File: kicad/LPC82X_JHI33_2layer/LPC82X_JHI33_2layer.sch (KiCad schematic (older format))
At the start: 24 parts, among them J1 Conn_02x09_Odd_Even, J2 Conn_02x09_Odd_Even, J3 JTAG_2X05, U1 LPC824M201JHI33, Y1 12MHz

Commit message: updated version number
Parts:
- N2: value 20181122 -> 20181123
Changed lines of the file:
@@
 P 4000 1650
 F 0 "N2" H 4000 1750 60  0000 C CNN
-F 1 "20181122" H 4000 1650 60  0000 C CNN
+F 1 "20181123" H 4000 1650 60  0000 C CNN
 F 2 "SquantorLabels:Label_version" H 4000 1650 60  0001 C CNN
 F 3 "" H 4000 1650 60  0001 C CNN

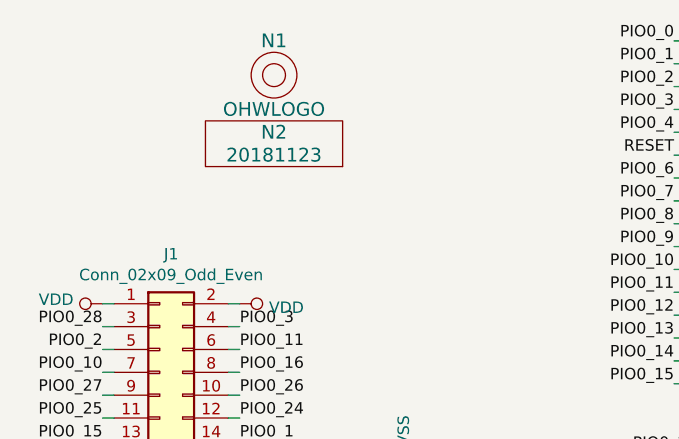
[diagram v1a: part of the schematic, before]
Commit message: updated versionnumber, fixed unrouted trace
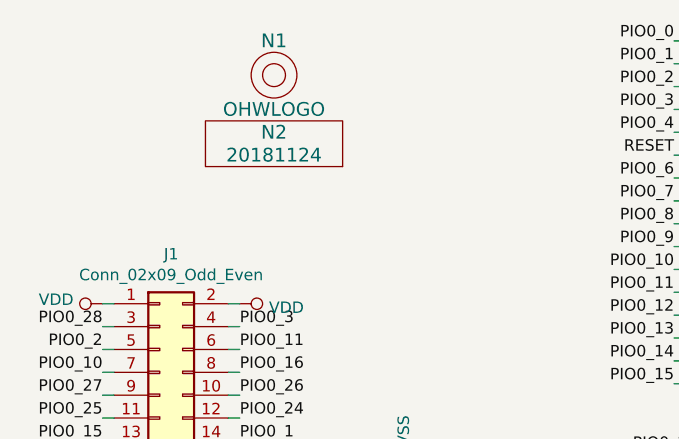
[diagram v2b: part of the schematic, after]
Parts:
- N2: value 20181123 -> 20181124
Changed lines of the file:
@@
 P 4000 1650
 F 0 "N2" H 4000 1750 60  0000 C CNN
-F 1 "20181123" H 4000 1650 60  0000 C CNN
+F 1 "20181124" H 4000 1650 60  0000 C CNN
 F 2 "SquantorLabels:Label_version" H 4000 1650 60  0001 C CNN
 F 3 "" H 4000 1650 60  0001 C CNN
